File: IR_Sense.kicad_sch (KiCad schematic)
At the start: 11 parts, among them J1 Conn_01x03, J2 Conn_01x02, Q1 SFH320, U2 LMV321

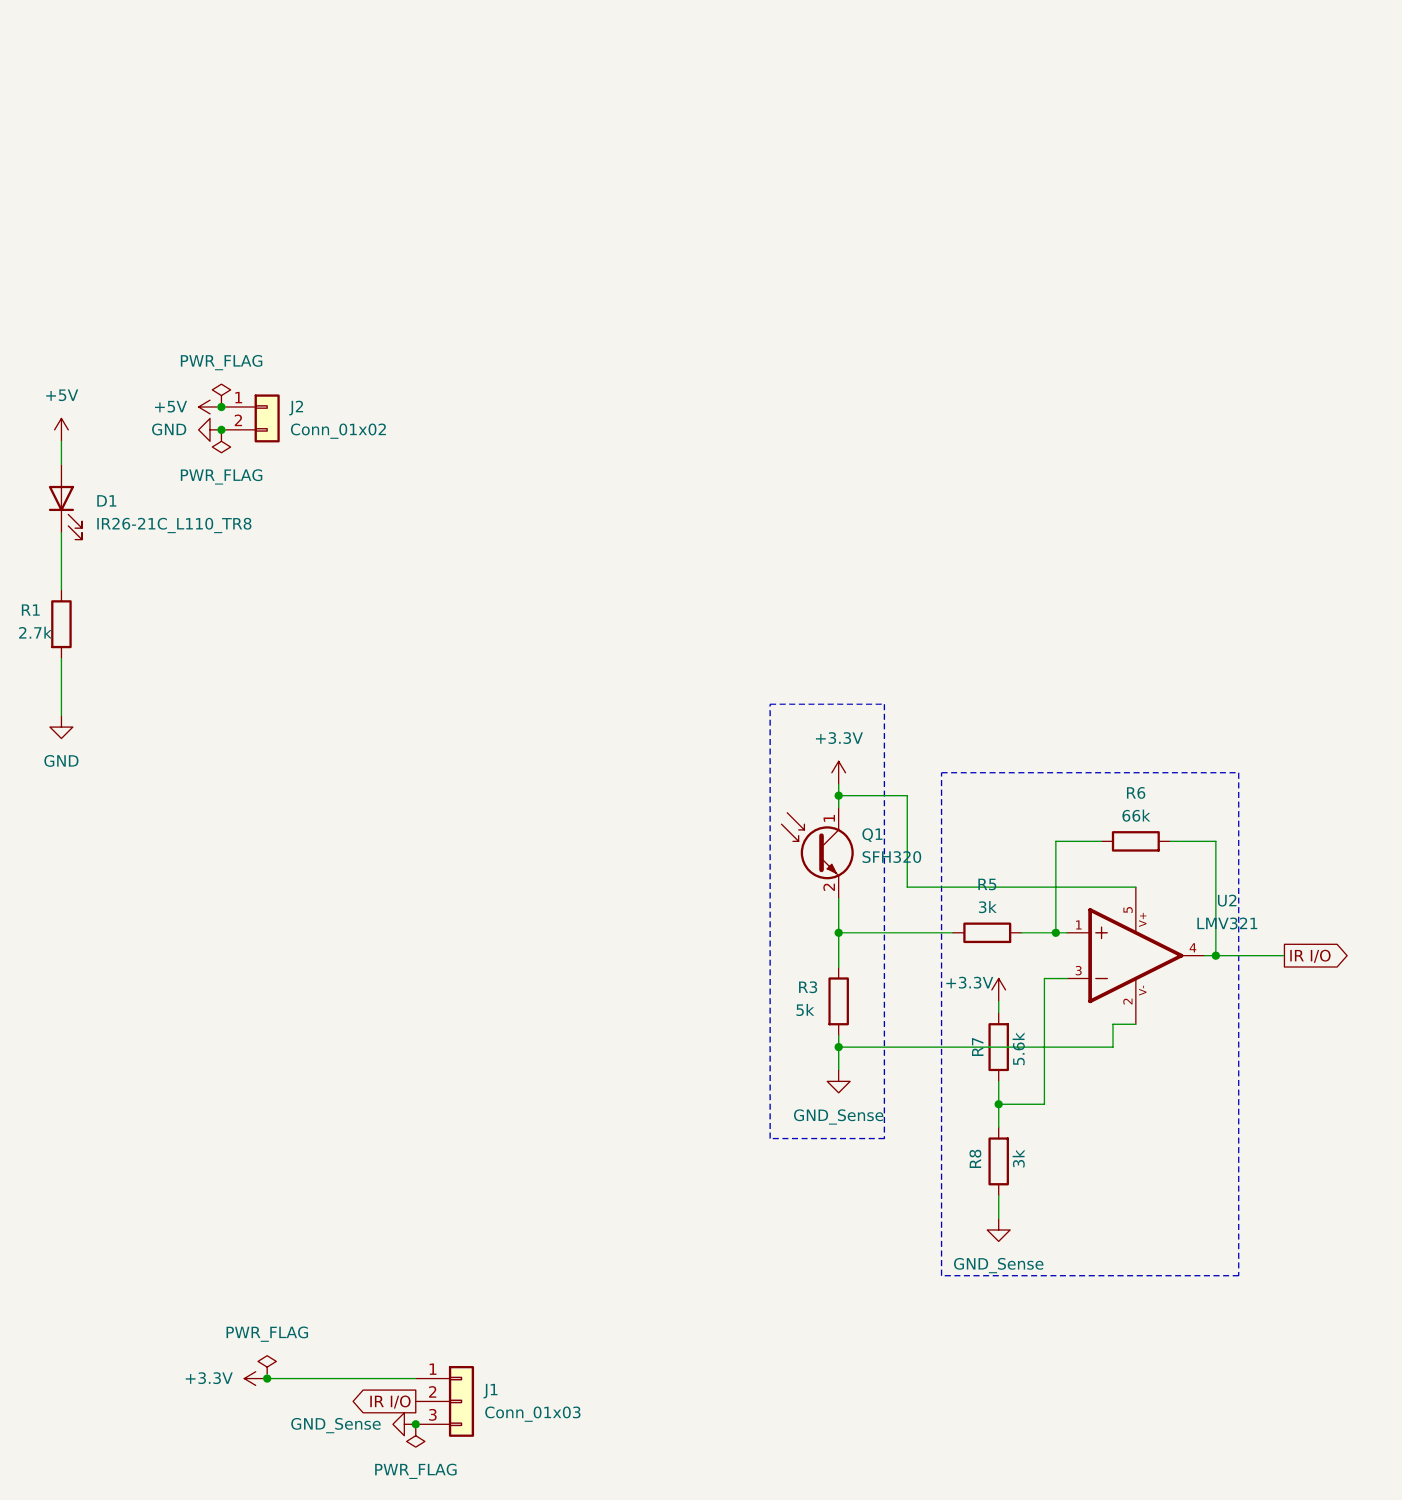
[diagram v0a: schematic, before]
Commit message: change IR diode and photo transistor
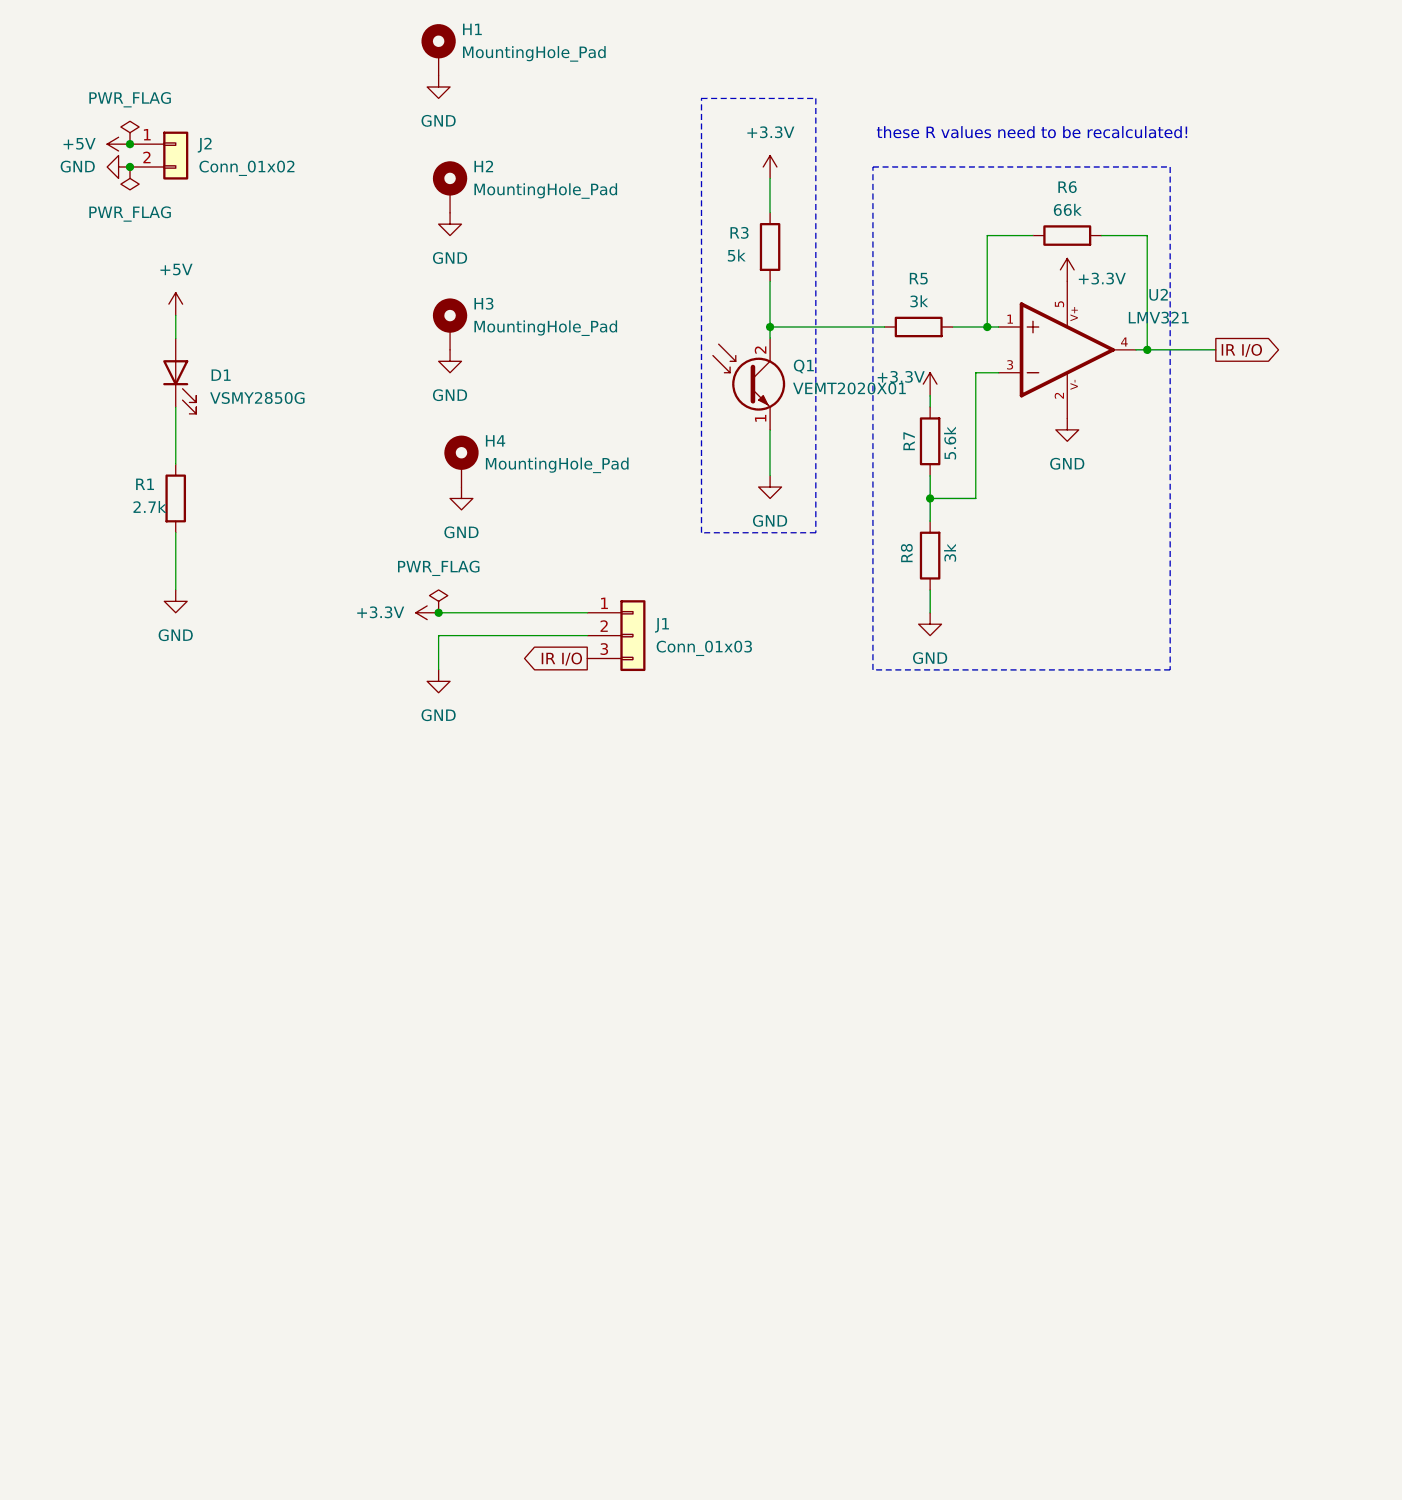
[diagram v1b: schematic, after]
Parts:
- removed Q1: SFH320, LED_SMD:LED_PLCC-2_3.4x3.0mm_KA, symbol Sensor_Optical:SFH320
- added H1, H2, H3, H4: MountingHole_Pad, MountingHole:MountingHole_2.2mm_M2_DIN965_Pad, symbol Mechanical:MountingHole_Pad
- added Q1: VEMT2020X01, IR_Sense:VSMY2850G_VEMT2020X01, symbol Device:Q_Photo_NPN_EC
- D1: value IR26-21C_L110_TR8 -> VSMY2850G; footprint LED_SMD:LED_1206_3216Metric -> IR_Sense:VSMY2850G_VEMT2020X01
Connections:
- net +3.3V: now also R3.1
- net GND: now also J1.2 (Pin_2), R8.1, U2.2, H1.1, H2.1, H3.1, H4.1, Q1.1 (E)
- net IR I/O: now also J1.3 (Pin_3); no longer J1.2 (Pin_2)
- net at R5.1: now also R3.2, Q1.2 (C); no longer R3.1
- removed net GND_Sense: J1.3 (Pin_3), R3.2, R8.1, U2.2
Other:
- note added: "these R values need to be recalculated!"
- moved on the sheet: D1, J1, J2, R1, R3, R5, R6, R7, R8, U2
